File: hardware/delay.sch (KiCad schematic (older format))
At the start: 19 parts

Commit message: more work on tdr schematic
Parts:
- removed C? (x5): .01 uF, symbol Device:C_Small
- removed R?: JMP, symbol Device:R_Small
- removed R?: DNI (2.2K), symbol Device:R_Small
- removed R?: DNI, symbol Device:R_Small
- removed R?: R_Small, symbol Device:R_Small
- removed RN? (x3): R_Pack04, symbol Device:R_Pack04
- removed TP? (x5): TestPoint, symbol Connector:TestPoint
- removed U?: MC100EP195B, symbol synth_lib:MC100EP195B
- added C? (x6): 100 pF, symbol Device:C_Small
- added C? (x6): 10 nF, symbol Device:C_Small
- added C?: 2.2 uF, symbol Device:C_Small
- added RN?: 22, symbol Device:R_Pack04
- U?: symbol synth_lib:NB6L295MMNG -> tdr-rescue:NB6L295MMNG-synth_lib
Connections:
- net labels added: +1V35, DELAY0_IN, DELAY0_OUT, DELAY1_IN, DELAY1_OUT, SCLK, SDIN, SLOAD, ~DELAY0_IN, ~DELAY0_OUT, ~DELAY1_IN, ~DELAY1_OUT
- net labels removed: D0, D1, D2, D3, D4, D5, D6, D7, D8, D9, DELAY_IN, DELAY_OUT, LEN, ~DELAY_IN, ~DELAY_OUT
- wire segments 77 -> 73
- no-connect marks 1 -> 0
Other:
- note added: "CML output, terminate with 50 ohms to Vcc"
- note added: "LVPECL CLK INPUT"
- note added: "VT = ~VT~ = Vcc - 2V"
- note added: "Vcc = 3.3 V, so, Vt = 1.3V?"
- note removed: "DO I CONNECT EP TO GROUND? NOT SPECIFIED.."
- note removed: "JMP FOR ECL INPUT\n"
- note removed: "POPULATE FOR LVTLL INPUT\n"
- note removed: "POPULATE FOR SINGLE ENDED INPUT"

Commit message: work on tdr schematic..
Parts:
- U?: symbol tdr-rescue:NB6L295MMNG-synth_lib -> tdr-rescue:NB6L295MMNG-synth_lib-tdr-rescue
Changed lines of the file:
@@
 $Descr A4 11693 8268
 encoding utf-8
-Sheet 8 9
+Sheet 6 8
 Title ""
 Date ""
@@
 $EndDescr
 $Comp
-L tdr-rescue:NB6L295MMNG-synth_lib U?
+L tdr-rescue:NB6L295MMNG-synth_lib-tdr-rescue U?
 U 1 1 5BCA9906
 P 5400 4000

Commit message: footprint assignment
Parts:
- C601: renamed from C?; footprint (none) -> Capacitors_SMD:C_0603
- C602, C603, C604, C605, C606, C607, C608, C609, C610, C611, C612, C613: renamed from C?; footprint (none) -> Capacitors_SMD:C_0402
- RN601: renamed from RN?; footprint (none) -> Resistors_SMD:R_Array_Convex_4x0402
- U601: renamed from U?; footprint (none) -> Housings_DFN_QFN:QFN-24-1EP_4x4mm_Pitch0.5mm

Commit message: work on tdr component placement
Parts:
- added C614, C615: 10 nF, Capacitors_SMD:C_0402, symbol Device:C_Small
- added R601, R602: 68, Resistors_SMD:R_0402, symbol Device:R_Small
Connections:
- net GND: now also C614.1, C615.2, R601.1, R602.1
- net +1V35: no longer names the net of U601.10 (~VT1), U601.7 (VT1)
- net +1V35: now also C615.1, R602.2; no longer U601.21 (~VT0), U601.24 (VT0)
- new net: C614.2, R601.2, U601.21 (~VT0), U601.24 (VT0)
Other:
- note removed: "LVPECL CLK INPUT"
- note removed: "VT = ~VT~ = Vcc - 2V"
- note removed: "Vcc = 3.3 V, so, Vt = 1.3V?"

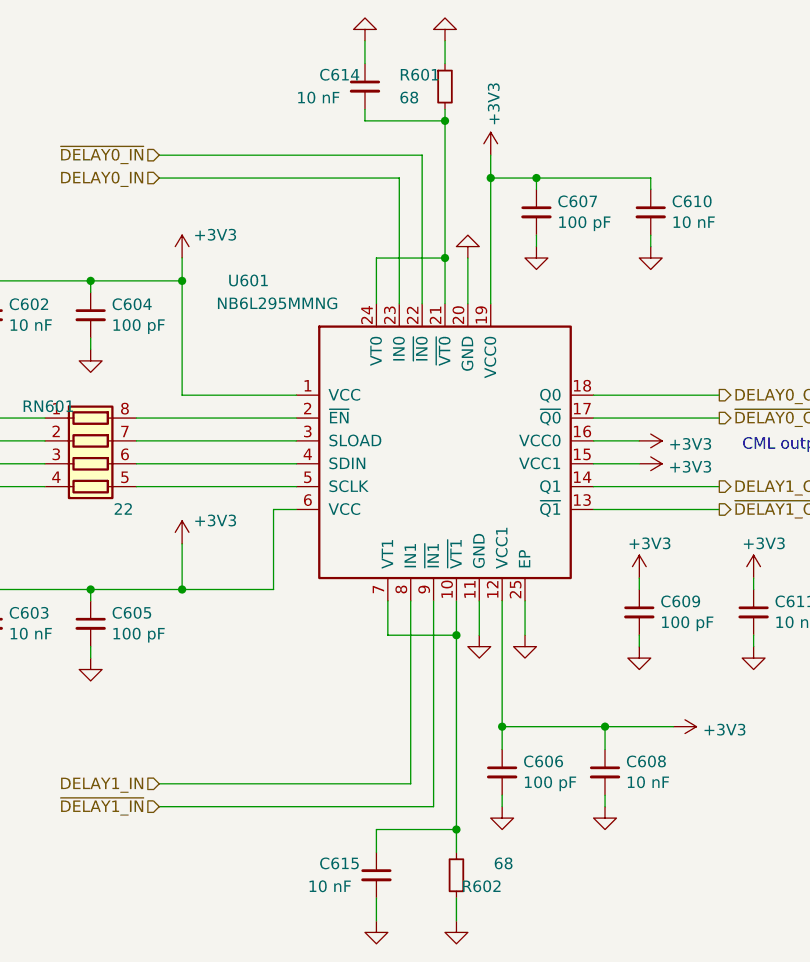
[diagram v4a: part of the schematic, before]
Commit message: fixed CML termination.. ready to order?
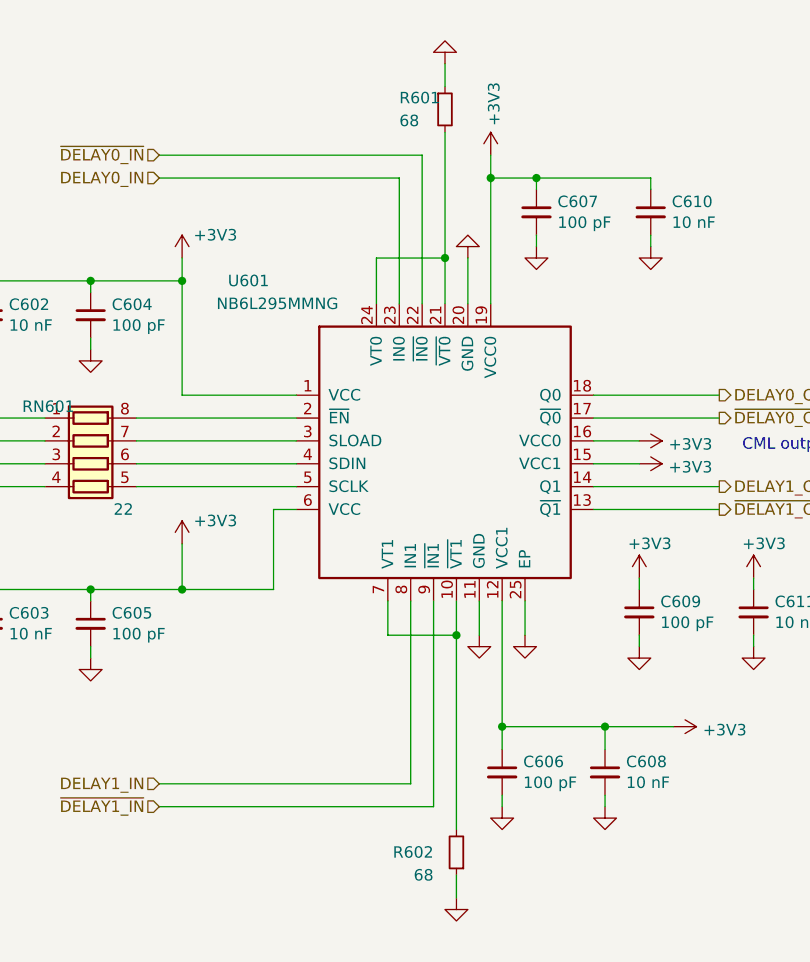
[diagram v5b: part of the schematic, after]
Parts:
- removed C614, C615: 10 nF, Capacitors_SMD:C_0402, symbol Device:C_Small
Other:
- moved on the sheet: R601, R602
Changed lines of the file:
@@
 Wire Wire Line
 	5100 3150 5400 3150
-Connection ~ 5400 3150
 $Comp
 L Device:R_Small R601
 U 1 1 5C19730A
-P 5400 2400
-F 0 "R601" H 5200 2450 50  0000 L CNN
-F 1 "68" H 5200 2350 50  0000 L CNN
-F 2 "Resistors_SMD:R_0402" H 5400 2400 50  0001 C CNN
-F 3 "~" H 5400 2400 50  0001 C CNN
-	1    5400 2400
+P 5400 2500
+F 0 "R601" H 5200 2550 50  0000 L CNN
+F 1 "68" H 5200 2450 50  0000 L CNN
+F 2 "Resistors_SMD:R_0402" H 5400 2500 50  0001 C CNN
+F 3 "~" H 5400 2500 50  0001 C CNN
+	1    5400 2500
 	1    0    0    -1
 $EndComp
-Wire Wire Line
-	5050 2500 5050 2550
-Wire Wire Line
-	5050 2550 5400 2550
-Wire Wire Line
-	5400 2550 5400 3150
 $Comp
 L power:GND #PWR?
 U 1 1 5C19959D
-P 5400 2200
+P 5400 2300
 AR Path="/5C19959D" Ref="#PWR?"  Part="1"
 AR Path="/5BC3A0BA/5C19959D" Ref="#PWR?"  Part="1"
@@
 AR Path="/5BC6A656/5C19959D" Ref="#PWR?"  Part="1"
 AR Path="/5BC64E97/5C19959D" Ref="#PWR0145"  Part="1"
-F 0 "#PWR0145" H 5400 1950 50  0001 C CNN
-F 1 "GND" H 5405 2027 50  0001 C CNN
-F 2 "" H 5400 2200 50  0001 C CNN
-F 3 "" H 5400 2200 50  0001 C CNN
-	1    5400 2200
+F 0 "#PWR0145" H 5400 2050 50  0001 C CNN
+F 1 "GND" H 5405 2127 50  0001 C CNN
+F 2 "" H 5400 2300 50  0001 C CNN
+F 3 "" H 5400 2300 50  0001 C CNN
+	1    5400 2300
 	-1   0    0    1
 $EndComp
 Wire Wire Line
-	5400 2200 5400 2300
+	5400 2300 5400 2400
 $Comp
 L Device:R_Small R602
 U 1 1 5C19E1C0
-P 5450 5850
-F 0 "R602" H 5250 5900 50  0000 L CNN
-F 1 "68" H 5200 5800 50  0000 L CNN
-F 2 "Resistors_SMD:R_0402" H 5450 5850 50  0001 C CNN
-F 3 "~" H 5450 5850 50  0001 C CNN
-	1    5450 5850
+P 5450 5750
+F 0 "R602" H 5550 5750 50  0000 L CNN
+F 1 "68" H 5550 5850 50  0000 L CNN
+F 2 "Resistors_SMD:R_0402" H 5450 5750 50  0001 C CNN
+F 3 "~" H 5450 5750 50  0001 C CNN
+	1    5450 5750
 	-1   0    0    1
 $EndComp
@@
 L power:GND #PWR?
 U 1 1 5C19E1C7
-P 5450 6050
+P 5450 5950
 AR Path="/5C19E1C7" Ref="#PWR?"  Part="1"
 AR Path="/5BC3A0BA/5C19E1C7" Ref="#PWR?"  Part="1"
@@
 AR Path="/5BC6A656/5C19E1C7" Ref="#PWR?"  Part="1"
 AR Path="/5BC64E97/5C19E1C7" Ref="#PWR0146"  Part="1"
-F 0 "#PWR0146" H 5450 5800 50  0001 C CNN
-F 1 "GND" H 5455 5877 50  0001 C CNN
-F 2 "" H 5450 6050 50  0001 C CNN
-F 3 "" H 5450 6050 50  0001 C CNN
-	1    5450 6050
+F 0 "#PWR0146" H 5450 5700 50  0001 C CNN
+F 1 "GND" H 5455 5777 50  0001 C CNN
+F 2 "" H 5450 5950 50  0001 C CNN
+F 3 "" H 5450 5950 50  0001 C CNN
+	1    5450 5950
 	1    0    0    -1
 $EndComp
 Wire Wire Line
-	5450 6050 5450 5950
+	5450 5950 5450 5850
 Wire Wire Line
 	5150 4800 5450 4800
 Wire Wire Line
-	5450 4800 5450 5650
+	5450 5650 5450 4800
 Connection ~ 5450 4800
-Connection ~ 5450 5650
 Wire Wire Line
-	5450 5650 5450 5750
-$Comp
-L Device:C_Small C?
-U 1 1 5C1B2DBA
-P 5100 5850
-AR Path="/5C1B2DBA" Ref="C?"  Part="1"
-AR Path="/5BC3A0BA/5C1B2DBA" Ref="C?"  Part="1"
-AR Path="/5BC3E552/5C1B2DBA" Ref="C?"  Part="1"
-AR Path="/5BC6A656/5C1B2DBA" Ref="C?"  Part="1"
-AR Path="/5BC64E97/5C1B2DBA" Ref="C615"  Part="1"
-F 0 "C615" H 4850 5900 50  0000 L CNN
-F 1 "10 nF" H 4800 5800 50  0000 L CNN
-F 2 "Capacitors_SMD:C_0402" H 5100 5850 50  0001 C CNN
-F 3 "~" H 5100 5850 50  0001 C CNN
-	1    5100 5850
-	1    0    0    -1
-$EndComp
-$Comp
-L power:GND #PWR?
-U 1 1 5C1B2E26
-P 5100 6050
-AR Path="/5C1B2E26" Ref="#PWR?"  Part="1"
-AR Path="/5BC3A0BA/5C1B2E26" Ref="#PWR?"  Part="1"
-AR Path="/5BC3E552/5C1B2E26" Ref="#PWR?"  Part="1"
-AR Path="/5BC6A656/5C1B2E26" Ref="#PWR?"  Part="1"
-AR Path="/5BC64E97/5C1B2E26" Ref="#PWR0147"  Part="1"
-F 0 "#PWR0147" H 5100 5800 50  0001 C CNN
-F 1 "GND" H 5105 5877 50  0001 C CNN
-F 2 "" H 5100 6050 50  0001 C CNN
-F 3 "" H 5100 6050 50  0001 C CNN
-	1    5100 6050
-	1    0    0    -1
-$EndComp
-$Comp
-L Device:C_Small C?
-U 1 1 5C1BE2D1
-P 5050 2400
-AR Path="/5C1BE2D1" Ref="C?"  Part="1"
-AR Path="/5BC3A0BA/5C1BE2D1" Ref="C?"  Part="1"
-AR Path="/5BC3E552/5C1BE2D1" Ref="C?"  Part="1"
-AR Path="/5BC6A656/5C1BE2D1" Ref="C?"  Part="1"
-AR Path="/5BC64E97/5C1BE2D1" Ref="C614"  Part="1"
-F 0 "C614" H 4850 2450 50  0000 L CNN
-F 1 "10 nF" H 4750 2350 50  0000 L CNN
-F 2 "Capacitors_SMD:C_0402" H 5050 2400 50  0001 C CNN
-F 3 "~" H 5050 2400 50  0001 C CNN
-	1    5050 2400
-	1    0    0    -1
-$EndComp
-$Comp
-L power:GND #PWR?
-U 1 1 5C1BE45F
-P 5050 2200
-AR Path="/5C1BE45F" Ref="#PWR?"  Part="1"
-AR Path="/5BC3A0BA/5C1BE45F" Ref="#PWR?"  Part="1"
-AR Path="/5BC3E552/5C1BE45F" Ref="#PWR?"  Part="1"
-AR Path="/5BC6A656/5C1BE45F" Ref="#PWR?"  Part="1"
-AR Path="/5BC64E97/5C1BE45F" Ref="#PWR0148"  Part="1"
-F 0 "#PWR0148" H 5050 1950 50  0001 C CNN
-F 1 "GND" H 5055 2027 50  0001 C CNN
-F 2 "" H 5050 2200 50  0001 C CNN
-F 3 "" H 5050 2200 50  0001 C CNN
-	1    5050 2200
-	-1   0    0    1
-$EndComp
-Wire Wire Line
-	5050 2200 5050 2300
-Wire Wire Line
-	5400 2500 5400 2550
-Connection ~ 5400 2550
-Wire Wire Line
-	5450 5650 5100 5650
-Wire Wire Line
-	5100 5650 5100 5750
-Wire Wire Line
-	5100 5950 5100 6050
+	5400 2600 5400 3150
+Connection ~ 5400 3150
 $EndSCHEMATC

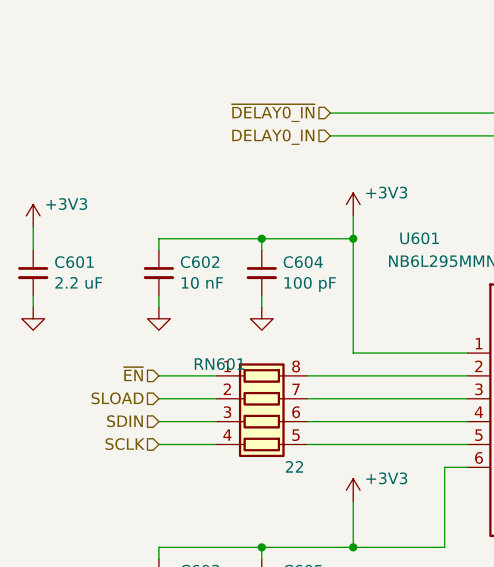
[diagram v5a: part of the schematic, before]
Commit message: schematic cleanup, BOM consolidation
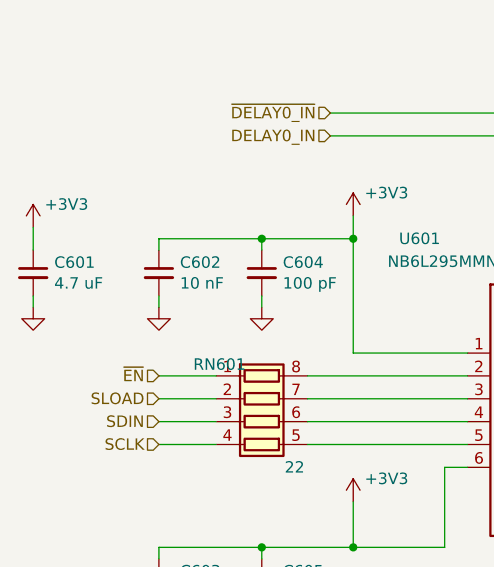
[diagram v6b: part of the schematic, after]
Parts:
- C601: value 2.2 uF -> 4.7 uF
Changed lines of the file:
@@
 AR Path="/5BC64E97/5BF51AAD" Ref="C601"  Part="1"
 F 0 "C601" H 2942 3446 50  0000 L CNN
-F 1 "2.2 uF" H 2942 3355 50  0000 L CNN
+F 1 "4.7 uF" H 2942 3355 50  0000 L CNN
 F 2 "Capacitors_SMD:C_0603" H 2850 3400 50  0001 C CNN
 F 3 "~" H 2850 3400 50  0001 C CNN
